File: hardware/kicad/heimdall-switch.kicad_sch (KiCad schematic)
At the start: 42 parts, among them J1 SWD (ARM 10-pin), J2 LOAD_OUT, J3 BATT_IN, J4 UI_BREAKOUT, Q1 AO3400A, Q2 BSS84, Q3 AO4407A, Q4 AO4407A, Q5 AO3400A, Q6 BSS84, SW1 KSC221J, U1 BT832, U2 TPS629206, Y1 32.768kHz

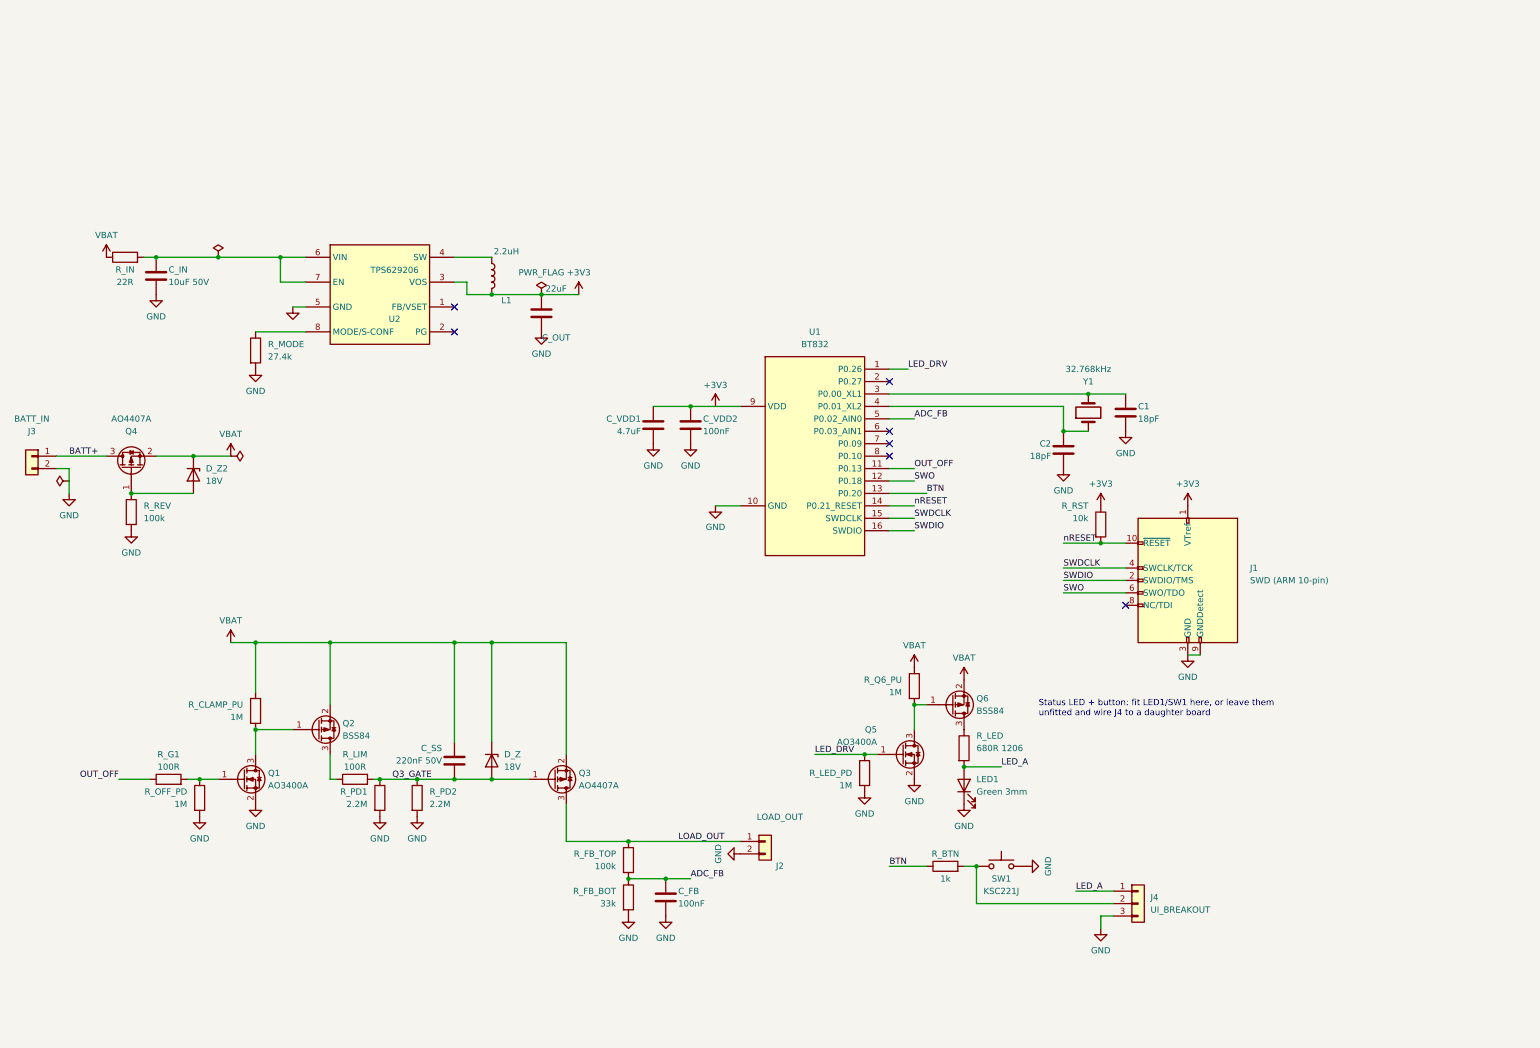
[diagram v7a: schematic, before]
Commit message: Add UI daughter board project; JST-XH breakout, KSC641J switch
New KiCad project hardware/kicad-ui/ for the optional LED + button
daughter board: schematic and routed 26x13mm 2-layer PCB (ERC 0/0, DRC
clean with schematic parity). LED and button on the front, JST-XH
header on the back so the board sits flat against the hull.

Main board: J4 is now a JST B3B-XH-A (crimped cable to the daughter
board), SW1 is the C&K KSC641J (matches KiCad's KSC6xxJ footprint).

Co-Authored-By: Claude Opus 5.5 <noreply@anthropic.com>
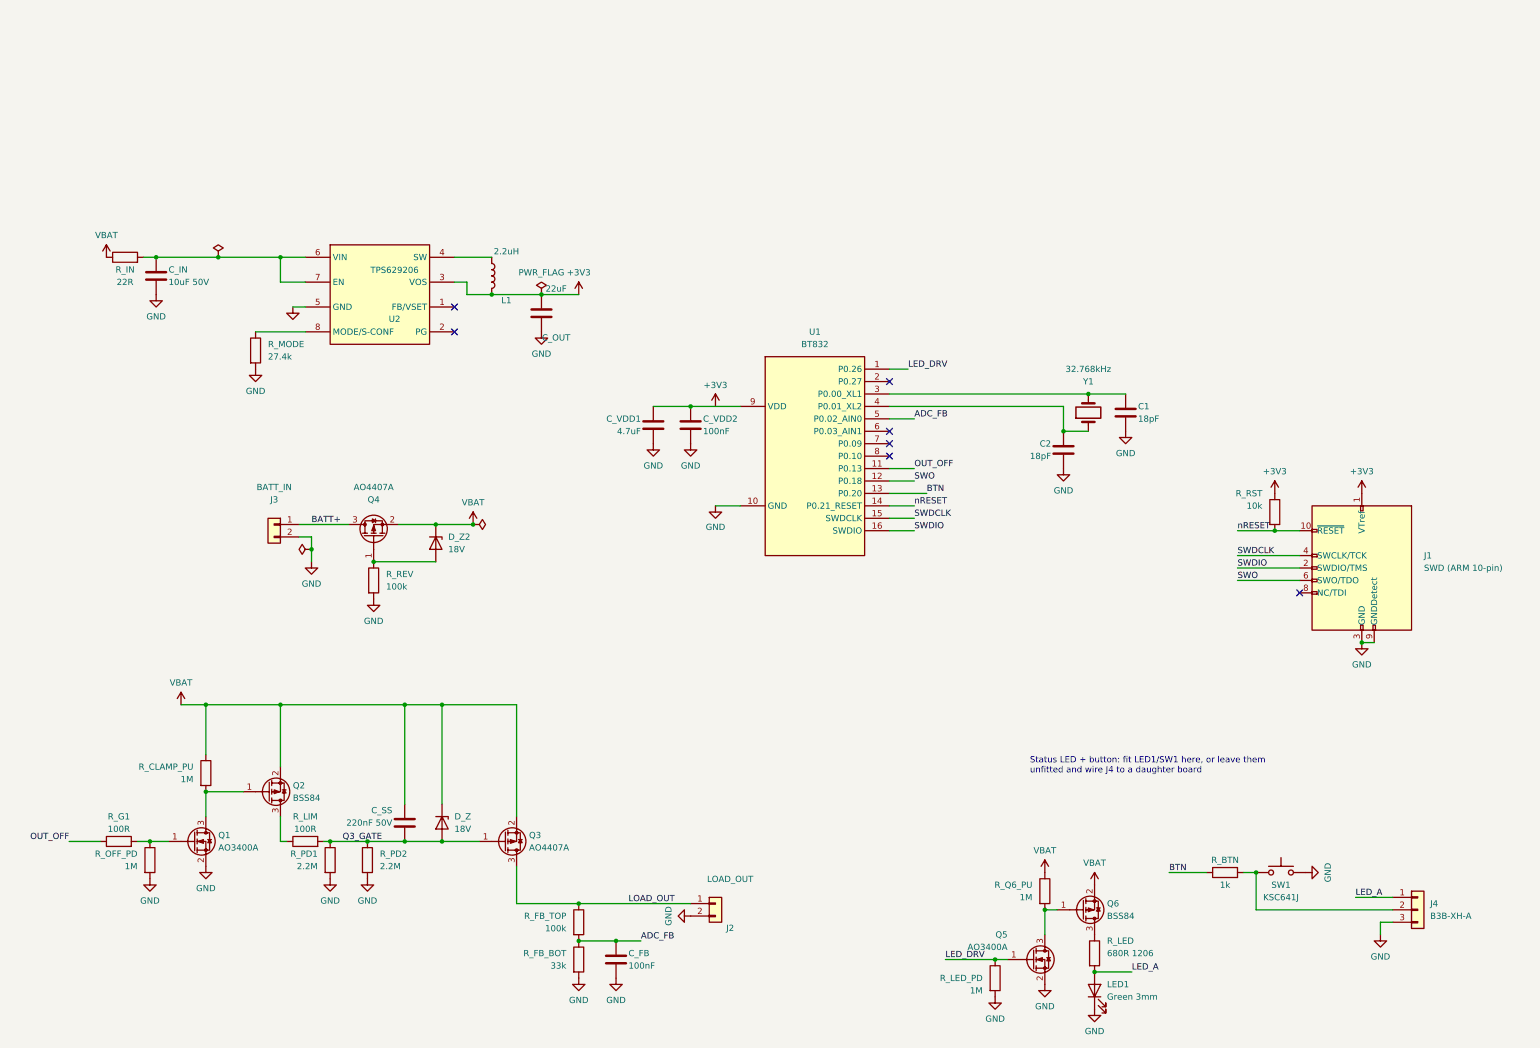
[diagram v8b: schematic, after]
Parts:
- J4: value UI_BREAKOUT -> B3B-XH-A; LCSC (none) -> C144394
- SW1: value KSC221J -> KSC641J; LCSC C221726 -> C226344
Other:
- moved on the sheet: C_FB, C_SS, D_Z, D_Z2, J1, J2, J3, J4, LED1, Q1, Q2, Q3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
